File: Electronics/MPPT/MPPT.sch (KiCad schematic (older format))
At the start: 73 parts, among them J1 Solar Array, J2 Battery, J3 Car Power, J4 CAN_In, J5 CAN_Out, Q1 200N25N, Q2 200N25N, SW1 RESET, U1 PDS1-S12-S9-M, U2 Nucleo_L432KC, U3 UCC37321, U4 INA213, U5 ADM3055E, U6 INA213, U7 CDSOT23-T24CAN

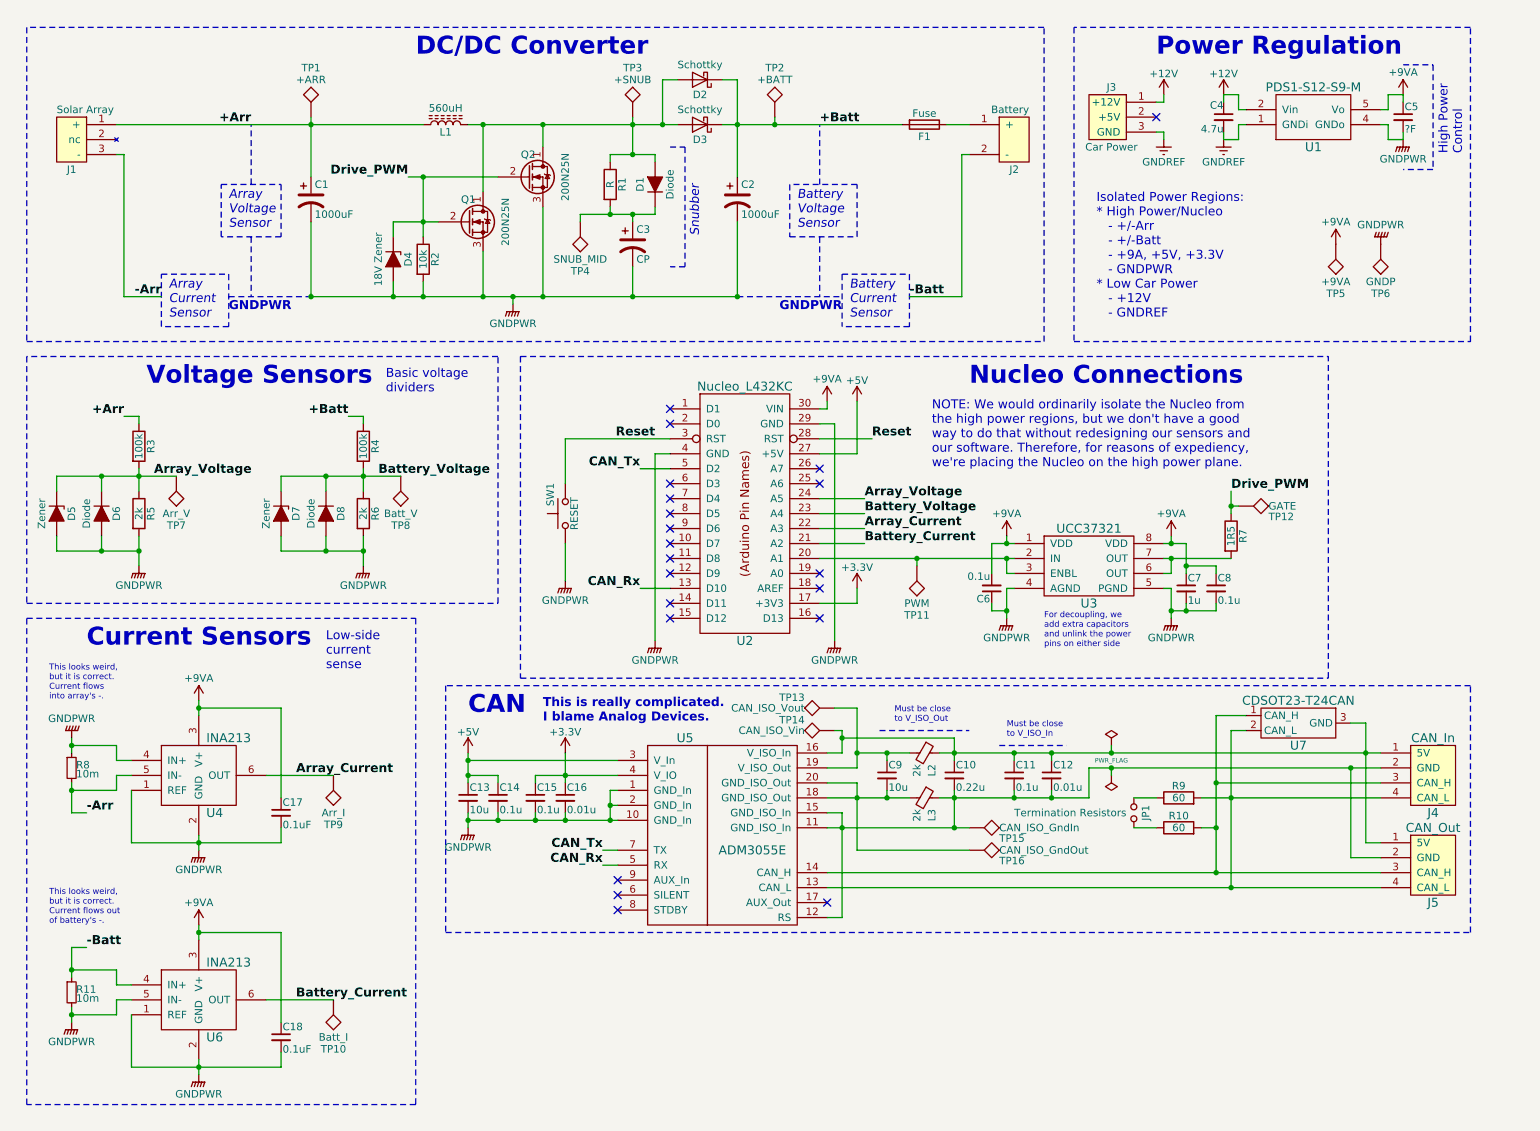
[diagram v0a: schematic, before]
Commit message: MPPT: Add CAN Address DIP switches
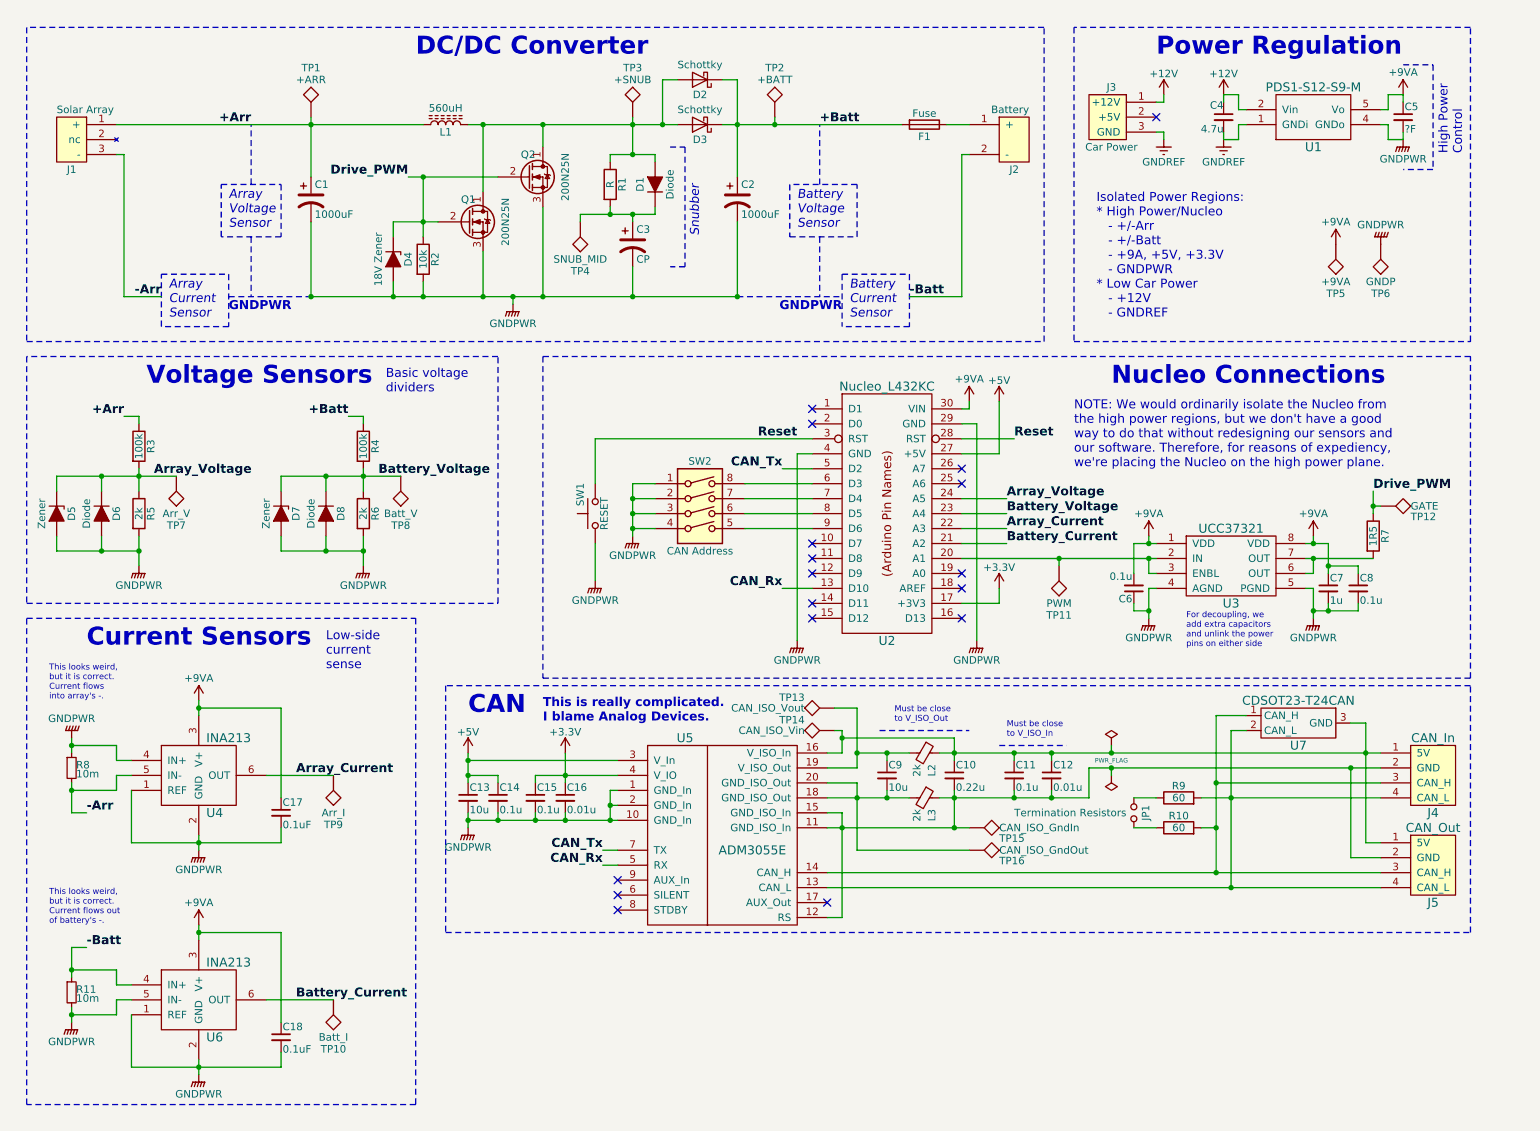
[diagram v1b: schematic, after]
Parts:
- added SW2: CAN Address, Buttons_Switches_THT:SW_DIP_x4_W7.62mm_Slide_LowProfile, symbol SW_DIP_x04
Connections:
- net GNDPWR: now also SW2.1, SW2.2, SW2.3, SW2.4
- net at U2.6 (D3): now also SW2.8
- net at U2.7 (D4): now also SW2.7
- net at U2.8 (D5): now also SW2.6
- net at U2.9 (D6): now also SW2.5
- no-connect marks 21 -> 17
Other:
- moved on the sheet: C6, C7, C8, R7, SW1, TP11, TP12, U2, U3

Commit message: MPPT: Add status LEDs and CAN Address DIP switches
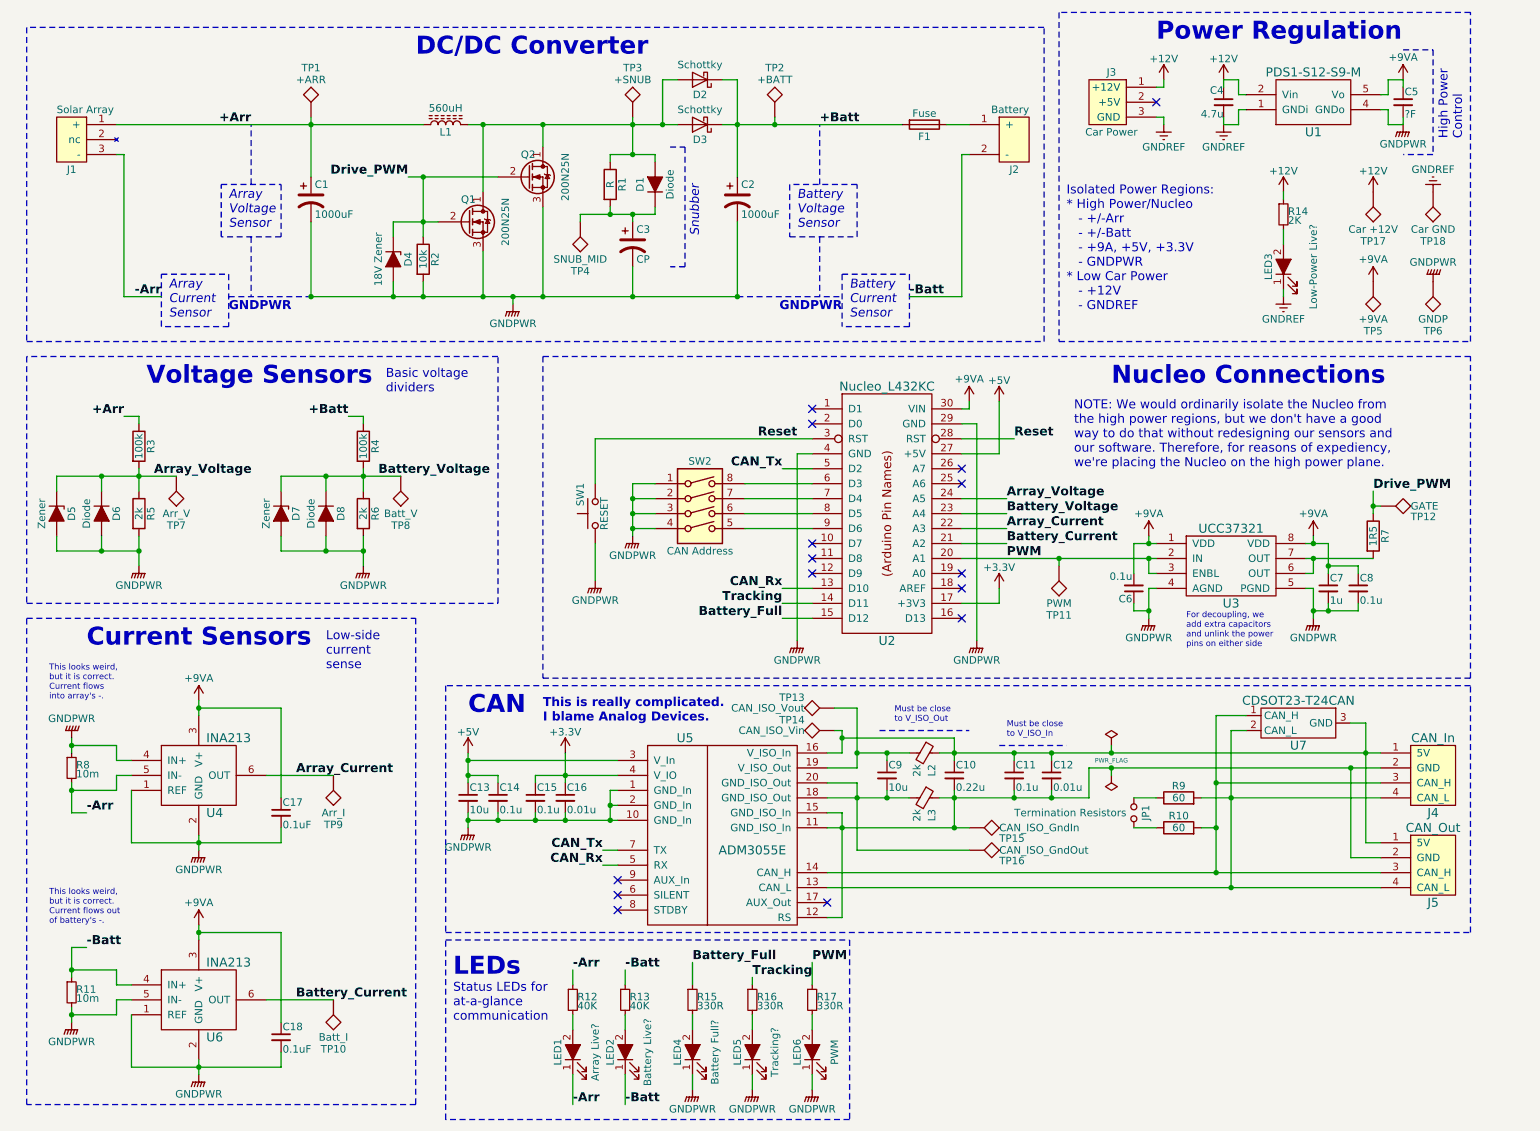
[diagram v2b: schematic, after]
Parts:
- added LED1: Array Live?, LEDs:LED_0805_HandSoldering, symbol LED_ALT
- added LED2: Battery Live?, LEDs:LED_0805_HandSoldering, symbol LED_ALT
- added LED3: Low-Power Live?, LEDs:LED_0805_HandSoldering, symbol LED_ALT
- added LED4: Battery Full?, LEDs:LED_0805_HandSoldering, symbol LED_ALT
- added LED5: Tracking?, LEDs:LED_0805_HandSoldering, symbol LED_ALT
- added LED6: PWM, LEDs:LED_0805_HandSoldering, symbol LED_ALT
- added R12, R13: 40K, Resistors_SMD:R_1206_HandSoldering, symbol R_Small
- added R14: 2K, Resistors_SMD:R_0805_HandSoldering, symbol R_Small
- added R15, R16, R17: 330R, Resistors_SMD:R_0805_HandSoldering, symbol R_Small
- added TP17: Car +12V, Measurement_Points:Test_Point_Keystone_5005-5009_Compact, symbol TEST
- added TP18: Car GND, Measurement_Points:Test_Point_Keystone_5005-5009_Compact, symbol TEST
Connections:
- net +12V: now also R14.1, TP17.1
- net -Arr: now also LED1.1 (K), R12.1
- net -Batt: now also LED2.1 (K), R13.1
- net GNDPWR: now also LED4.1 (K), LED5.1 (K), LED6.1 (K)
- net GNDREF: now also LED3.1 (K), TP18.1
- net Tracking: now reaches U2.14 (D11)
- net Tracking: now also R16.1
- net Battery_Full: now reaches U2.15 (D12)
- net Battery_Full: now also R15.1
- net PWM: now reaches TP11.1, U2.20 (A1), U3.2 (IN), U3.3 (ENBL)
- net PWM: now also R17.1
- new net: LED4.2 (A), R15.2
- new net: LED5.2 (A), R16.2
- new net: LED1.2 (A), R12.2
- new net: LED2.2 (A), R13.2
- new net: LED6.2 (A), R17.2
- new net: LED3.2 (A), R14.2
- no-connect marks 17 -> 15
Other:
- note added: "LEDs"
- note added: "Status LEDs for\nat-a-glance\ncommunication"
- moved on the sheet: C4, C5, J3, TP5, TP6, U1

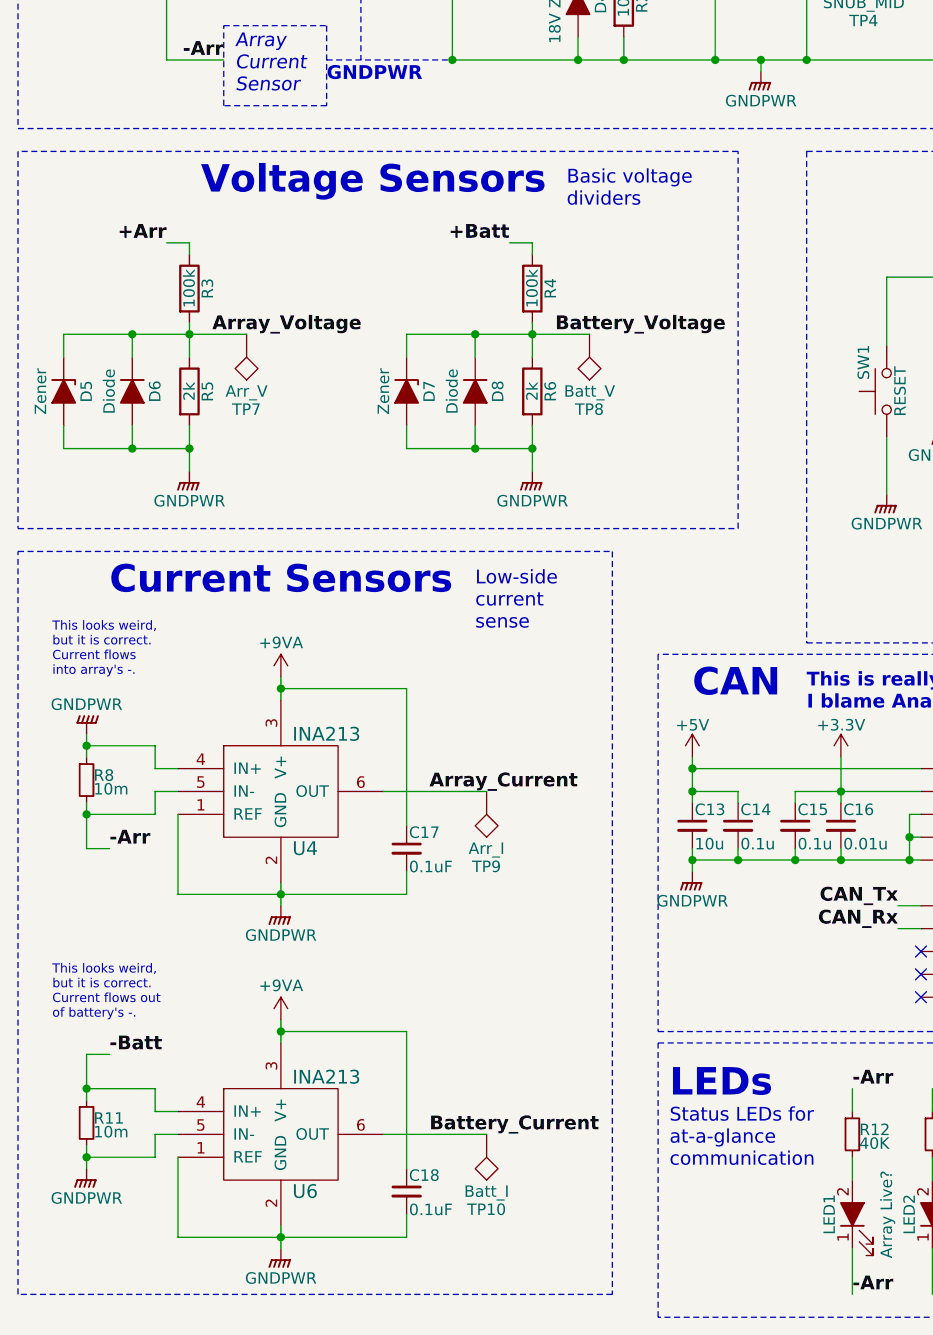
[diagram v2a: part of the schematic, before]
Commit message: MPPT: Add pads for RC filter on voltage and current sensors.
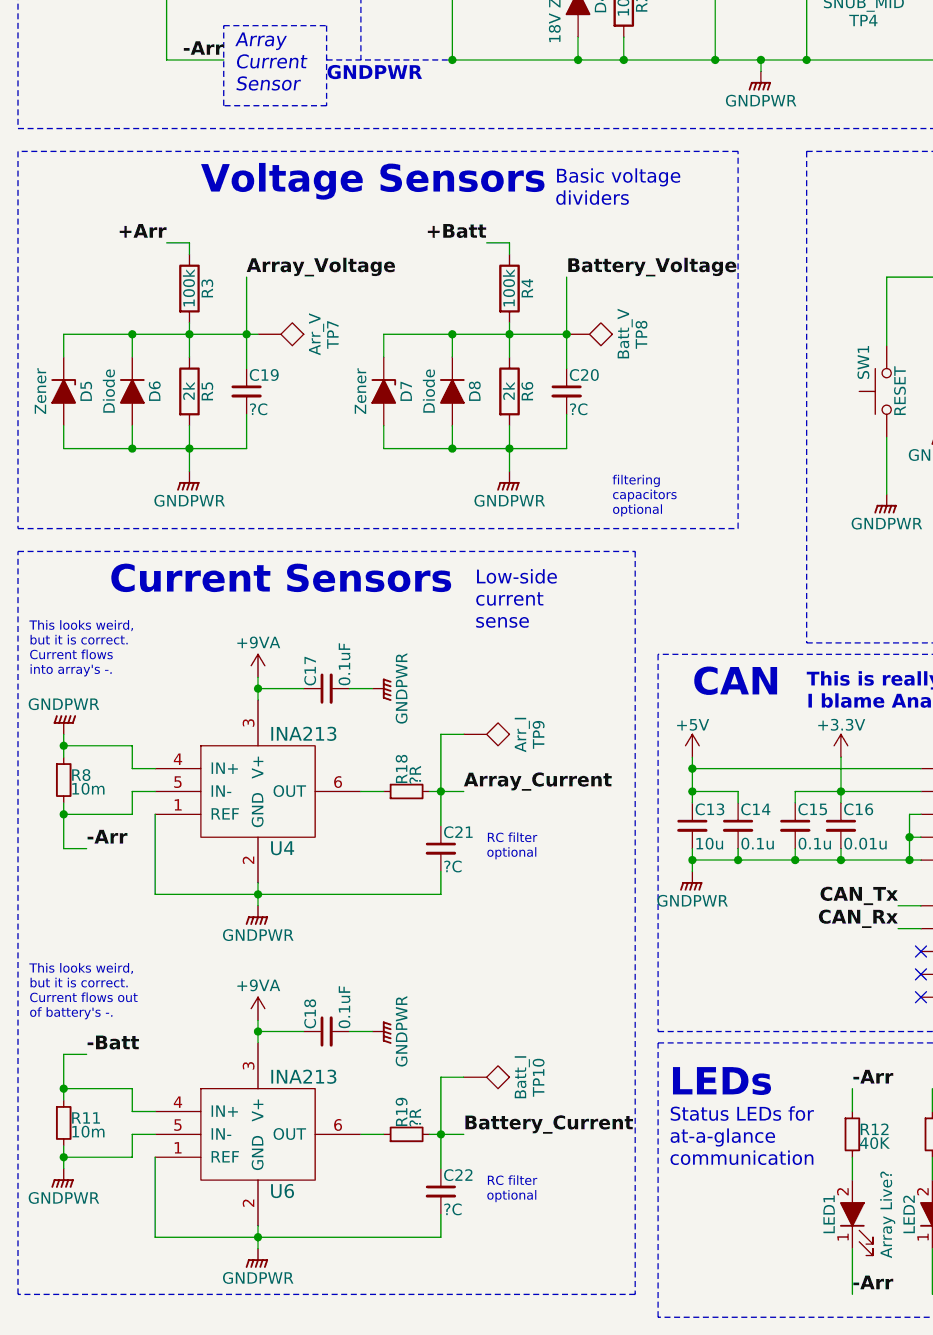
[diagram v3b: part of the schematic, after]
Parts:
- added C19, C20: ?C, Capacitors_SMD:C_1206_HandSoldering, symbol C_Small
- added C21, C22: ?C, Capacitors_SMD:C_0805_HandSoldering, symbol C_Small
- added R18, R19: ?R, Resistors_SMD:R_0805_HandSoldering, symbol R_Small
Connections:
- net Array_Current: now also C21.1, R18.2; no longer U4.6 (OUT)
- net Array_Voltage: now also C19.1
- net Battery_Current: now also C22.1, R19.2; no longer U6.6 (OUT)
- net Battery_Voltage: now also C20.1
- net GNDPWR: now also C19.2, C20.2, C21.2, C22.2
- new net: R18.1, U4.6 (OUT)
- new net: R19.1, U6.6 (OUT)
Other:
- note added: "RC filter\noptional"
- note added: "\nfiltering\ncapacitors\noptional"
- moved on the sheet: C17, C18, D7, D8, R11, R4, R6, R8, TP10, TP7, TP8, TP9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
